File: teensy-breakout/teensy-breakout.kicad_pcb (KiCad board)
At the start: 2 copper layers, 1 part, among them U1 Teensy4.1

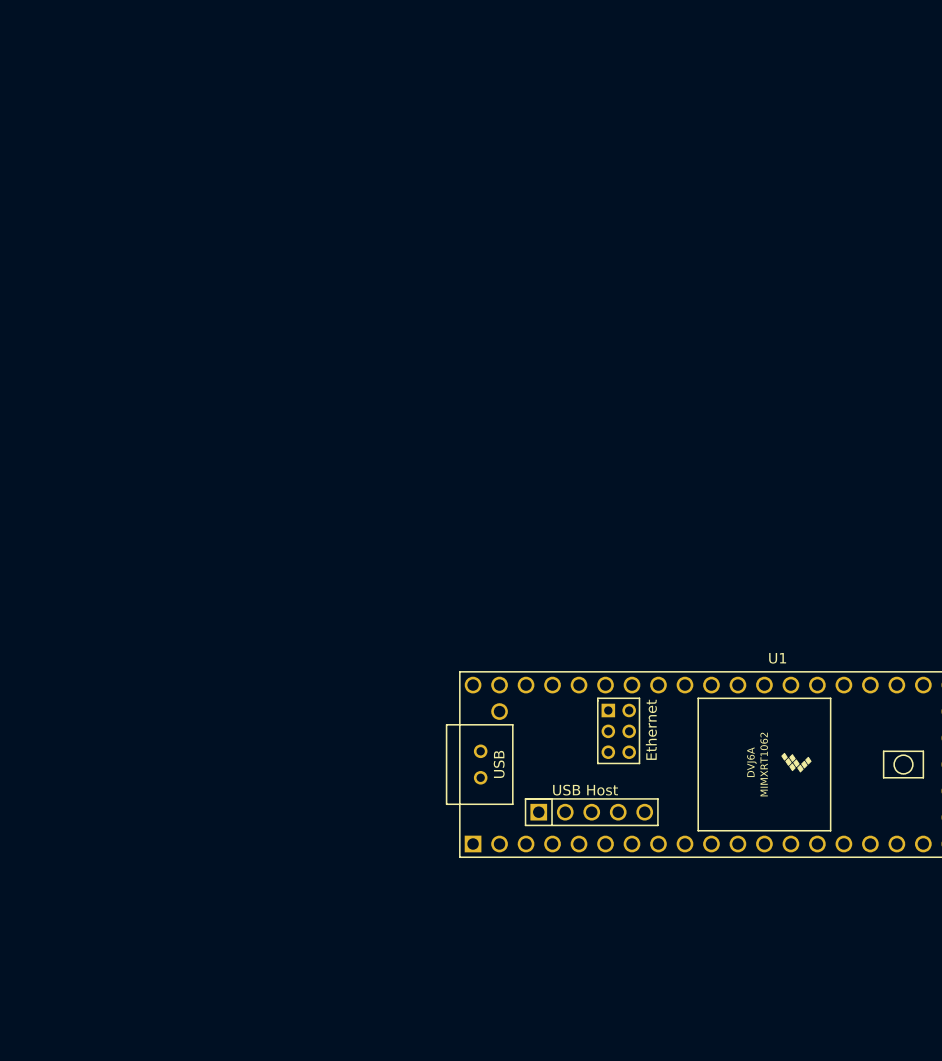
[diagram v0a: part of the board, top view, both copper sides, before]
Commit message: Initial work on teensy brakeout PCB
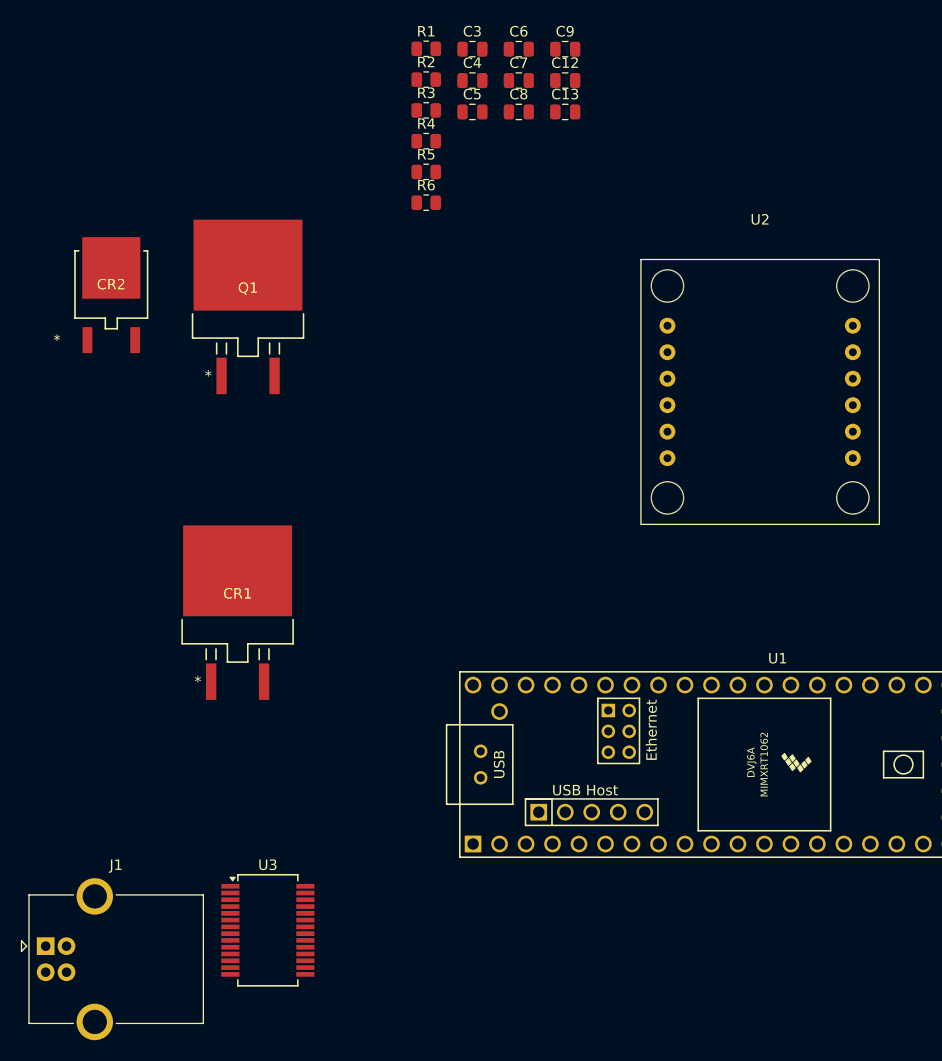
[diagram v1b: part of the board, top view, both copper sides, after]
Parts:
- added C12: 100n, Capacitor_SMD:C_0805_2012Metric, F.Cu at (85.9, 34.8)
- added C13: 10u, Capacitor_SMD:C_0805_2012Metric, F.Cu at (85.9, 37.8)
- added C3: 10u, Capacitor_SMD:C_0805_2012Metric, F.Cu at (77.0, 31.8)
- added C4: 1u, Capacitor_SMD:C_0805_2012Metric, F.Cu at (77.0, 34.8)
- added C5: 10u, Capacitor_SMD:C_0805_2012Metric, F.Cu at (77.0, 37.8)
- added C6: 1u, Capacitor_SMD:C_0805_2012Metric, F.Cu at (81.5, 31.8)
- added C7: 10u, Capacitor_SMD:C_0805_2012Metric, F.Cu at (81.5, 34.8)
- added C8: 10u, Capacitor_SMD:C_0805_2012Metric, F.Cu at (81.5, 37.8)
- added C9: 100n, Capacitor_SMD:C_0805_2012Metric, F.Cu at (85.9, 31.8)
- added CR1: L7805CD2T-TR, Custom:D2PAKSMD_2L_STD-ST_STM, F.Cu at (54.5, 84.0)
- added CR2: MBRD10100CT-13, Custom:TO252DPAK_DIO, F.Cu at (42.4, 54.3)
- added J1: USB_B, Connector_USB:USB_B_OST_USB-B1HSxx_Horizontal, F.Cu at (36.1, 117.8)
- added Q1: IRL530NSTRLPBF, Custom:D2PAKSMD_2L_STD-ST_STM, F.Cu at (55.5, 54.7)
- added R1: 1k, Resistor_SMD:R_0805_2012Metric, F.Cu at (72.6, 31.8)
- added R2: 10k, Resistor_SMD:R_0805_2012Metric, F.Cu at (72.6, 34.7)
- added R3: 270, Resistor_SMD:R_0805_2012Metric, F.Cu at (72.6, 37.6)
- added R4: 270, Resistor_SMD:R_0805_2012Metric, F.Cu at (72.6, 40.6)
- added R5: 2k, Resistor_SMD:R_0805_2012Metric, F.Cu at (72.6, 43.5)
- added R6: 2k, Resistor_SMD:R_0805_2012Metric, F.Cu at (72.6, 46.5)
- added U2: ~, Custom:BNO085, F.Cu at (104.6, 64.7)
- added U3: FT232RL, Package_SO:SSOP-28_5.3x10.2mm_P0.65mm, F.Cu at (57.4, 116.3)
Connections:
- U1 pad 1: unconnected-(U1-GND-Pad1) -> GND
- U1 pad 15: unconnected-(U1-3V3-Pad15) -> +3V3
- U1 pad 2: unconnected-(U1-0_RX1_CRX2_CS1-Pad2) -> /UART1 RX
- U1 pad 3: unconnected-(U1-1_TX1_CTX2_MISO1-Pad3) -> /UART1 TX
- U1 pad 34: unconnected-(U1-GND-Pad34) -> GND
- U1 pad 4: unconnected-(U1-2_OUT2-Pad4) -> /UART1 RTS
- U1 pad 40: unconnected-(U1-18_A4_SDA-Pad40) -> /I2C0_SDA
- U1 pad 41: unconnected-(U1-19_A5_SCL-Pad41) -> /I2C0_SCL
- U1 pad 46: unconnected-(U1-3V3-Pad46) -> +3V3
- U1 pad 47: unconnected-(U1-GND-Pad47) -> GND
- U1 pad 48: unconnected-(U1-VIN-Pad48) -> +5V
- U1 pad 5: unconnected-(U1-3_LRCLK2-Pad5) -> /UART1 CTS
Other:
- board outline added: 20.9 x 23.4 mm

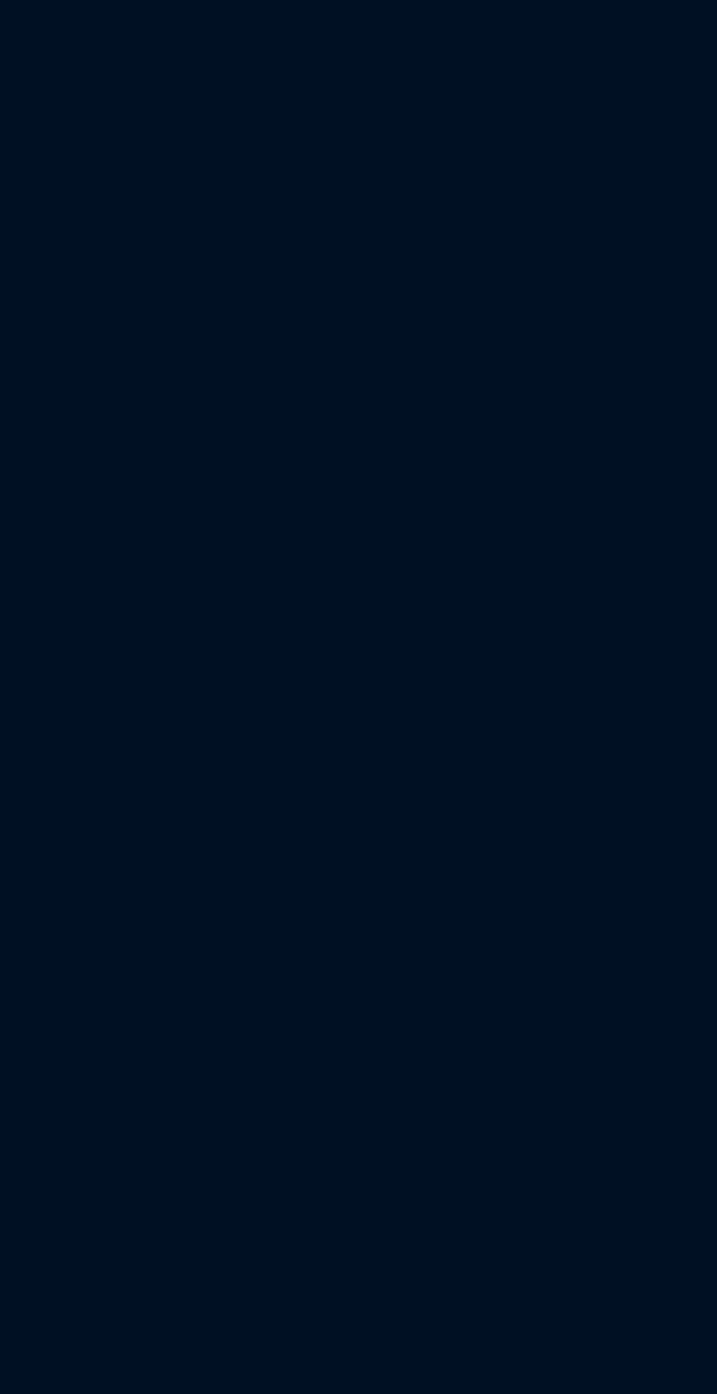
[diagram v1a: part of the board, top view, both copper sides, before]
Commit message: Started working to integrate ZED-F9P and feather. Still need to make Zed-F9P footprint.
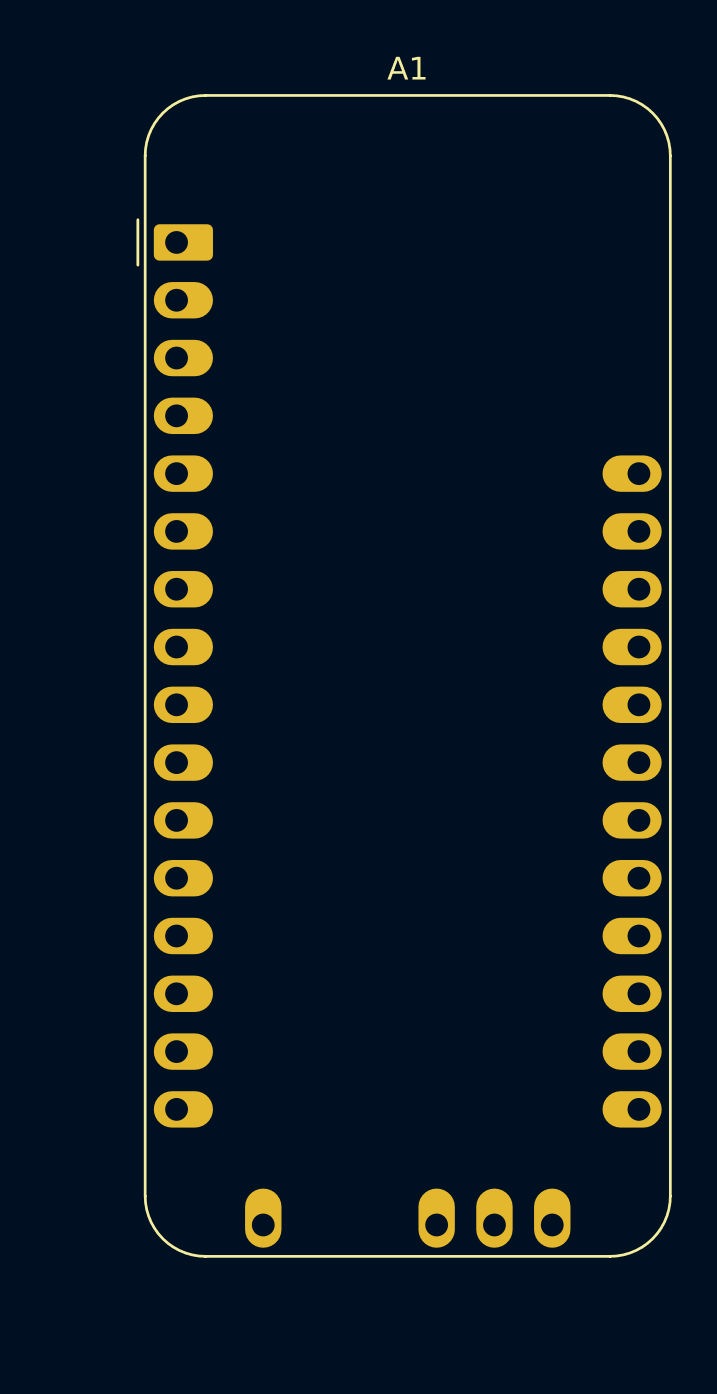
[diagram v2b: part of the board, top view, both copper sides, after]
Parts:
- added A1: Adafruit_Feather_M0_RFM9x_LoRa_Radio, Module:Adafruit_Feather_M0_RFM, F.Cu at (136.2, 30.4)

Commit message: More work done on schematic, seems good to me
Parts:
- added C14: 10u, Capacitor_SMD:C_0805_2012Metric_Pad1.18x1.45mm_HandSolder, F.Cu at (67.5, 31.4)
- added C15: 1u, Capacitor_SMD:C_0805_2012Metric_Pad1.18x1.45mm_HandSolder, F.Cu at (67.5, 34.4)
- added C16: 10u, Capacitor_SMD:C_0805_2012Metric_Pad1.18x1.45mm_HandSolder, F.Cu at (83.0, 44.0)
- added C17: 1u, Capacitor_SMD:C_0805_2012Metric_Pad1.18x1.45mm_HandSolder, F.Cu at (83.0, 47.0)
- added C18: 1u, Capacitor_SMD:C_0805_2012Metric_Pad1.18x1.45mm_HandSolder, F.Cu at (67.5, 37.5)
- added C19: 1u, Capacitor_SMD:C_0805_2012Metric_Pad1.18x1.45mm_HandSolder, F.Cu at (67.5, 40.5)
- added C20: 100u, Capacitor_SMD:C_0805_2012Metric_Pad1.18x1.45mm_HandSolder, F.Cu at (77.0, 40.5)
- added C21: 10u, Capacitor_SMD:C_0805_2012Metric_Pad1.18x1.45mm_HandSolder, F.Cu at (67.5, 43.5)
- added C22: 1u, Capacitor_SMD:C_0805_2012Metric_Pad1.18x1.45mm_HandSolder, F.Cu at (67.5, 46.5)
- added C23: 10u, Capacitor_SMD:C_0805_2012Metric_Pad1.18x1.45mm_HandSolder, F.Cu at (67.5, 49.5)
- added C24: 10u, Capacitor_SMD:C_0805_2012Metric_Pad1.18x1.45mm_HandSolder, F.Cu at (67.5, 52.5)
- added J10: 1988820, Custom:CONN_1988820, F.Cu at (53.7, 154.8)
- added J2: 1988820, Custom:CONN_1988820, F.Cu at (28.5, 82.2)
- added J3: 1988820, Custom:CONN_1988820, F.Cu at (28.5, 96.8)
- added J4: 1988820, Custom:CONN_1988820, F.Cu at (28.5, 111.4)
- added J5: 1988820, Custom:CONN_1988820, F.Cu at (28.5, 126.0)
- added J6: 1988820, Custom:CONN_1988820, F.Cu at (28.5, 140.6)
- added J7: 1988820, Custom:CONN_1988820, F.Cu at (28.5, 155.2)
- added J8: 1988833, Custom:CONN_1988833, F.Cu at (58.7, 140.2)
- added J9: 1988956, Custom:CONN_1988956, F.Cu at (64.3, 153.5)
- added R10: 10k, Resistor_SMD:R_0805_2012Metric_Pad1.20x1.40mm_HandSolder, F.Cu at (77.5, 51.0)
- added R8: 1k, Resistor_SMD:R_0805_2012Metric_Pad1.20x1.40mm_HandSolder, F.Cu at (77.5, 45.1)
- added R9: 10k, Resistor_SMD:R_0805_2012Metric_Pad1.20x1.40mm_HandSolder, F.Cu at (77.5, 48.0)
- added U5: ~, Custom:RFM69HCW Adafruit Breakout, F.Cu at (177.4, 115.4)
- added U6: ICL7667CBAZA-TDKR, Custom:SOIC8_4X5_INR, F.Cu at (61.3, 160.1)
- C12: value 100n -> 1u; footprint Capacitor_SMD:C_0805_2012Metric -> Capacitor_SMD:C_0805_2012Metric_Pad1.18x1.45mm_HandSolder
- C13, C3, C4, C5, C6, C7, C8, C9: footprint Capacitor_SMD:C_0805_2012Metric -> Capacitor_SMD:C_0805_2012Metric_Pad1.18x1.45mm_HandSolder
- R3, R4, R5, R6: footprint Resistor_SMD:R_0805_2012Metric -> Resistor_SMD:R_0805_2012Metric_Pad1.20x1.40mm_HandSolder
- moved U3 0.50 mm to (56.9, 116.3)
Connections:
- R1 pad 1: unconnected-(R1-Pad1) -> /BRAKE
- U1 pad 10: unconnected-(U1-8_TX2_IN1-Pad10) -> /UART2_TX
- U1 pad 12: unconnected-(U1-10_CS_MQSR-Pad12) -> /RF_CS
- U1 pad 13: unconnected-(U1-11_MOSI_CTX1-Pad13) -> /MOSI
- U1 pad 14: unconnected-(U1-12_MISO_MQSL-Pad14) -> /MISO
- U1 pad 18: unconnected-(U1-26_A12_MOSI1-Pad18) -> /BRAKE
- U1 pad 19: unconnected-(U1-27_A13_SCK1-Pad19) -> /PUL
- U1 pad 28: unconnected-(U1-36_CS-Pad28) -> /RF_G0
- U1 pad 29: unconnected-(U1-37_CS-Pad29) -> /RF_RST
- U1 pad 30: unconnected-(U1-38_CS1_IN1-Pad30) -> /DIR
- U1 pad 31: unconnected-(U1-39_MISO1_OUT1A-Pad31) -> /ALM
- U1 pad 35: unconnected-(U1-13_SCK_LED-Pad35) -> /SCK
- U1 pad 9: unconnected-(U1-7_RX2_OUT1A-Pad9) -> /UART2_RX
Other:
- board size 20.9 x 23.4 mm -> 25.4 x 29.2 mm

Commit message: Work on layout & wiring. Mostly done, need to look it over. It's very messy :(
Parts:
- added C1: 100u, Custom:CAP_A765EB_KEM, F.Cu at (188.2, 52.5)
- added C2: 100u, Custom:CAP_A765EB_KEM, F.Cu at (208.9, 66.5)
- added C25: 1u, Capacitor_SMD:C_0805_2012Metric_Pad1.18x1.45mm_HandSolder, F.Cu at (114.0, 35.5)
- added CR3: L7805CD2T-TR, Custom:D2PAKSMD_2L_STD-ST_STM, F.Cu at (213.5, 122.0)
- added CR4: L7805CD2T-TR, Custom:D2PAKSMD_2L_STD-ST_STM, F.Cu at (86.5, 80.5)
- added D1: BLUE, LED_SMD:LED_0805_2012Metric, F.Cu at (57.6, 72.1)
- added D2: BLUE, LED_SMD:LED_0805_2012Metric, F.Cu at (61.6, 72.0)
- added D3: LED, LED_SMD:LED_0805_2012Metric_Pad1.15x1.40mm_HandSolder, F.Cu at (227.4, 99.0)
- added D4: GREEN, LED_SMD:LED_0805_2012Metric, F.Cu at (107.4, 100.0)
- added J11: 1988817, Custom:CONN_1988817, F.Cu at (82.4, 30.2)
- added J12: 1988817, Custom:CONN_1988817, F.Cu at (16.5, 133.2)
- added J13: 1988817, Custom:CONN_1988817, F.Cu at (16.7, 178.6)
- added J14: 1988817, Custom:CONN_1988817, F.Cu at (72.6, 191.8)
- added J15: 1988820, Custom:CONN_1988820, F.Cu at (58.8, 30.0)
- added J17: 1988956, Custom:CONN_1988956, F.Cu at (251.3, 31.6)
- added J18: 1988817, Custom:CONN_1988817, F.Cu at (161.9, 30.2)
- added J19: 1989010, Custom:PHOENIX_1989010, F.Cu at (25.8, 194.4)
- added J20: 1989010, Custom:PHOENIX_1989010, F.Cu at (151.5, 27.6)
- added J21: 1988956, Custom:CONN_1988956, F.Cu at (186.4, 29.2)
- added J22: 1988817, Custom:CONN_1988817, F.Cu at (213.2, 191.5)
- added J9: 1988956, Custom:CONN_1988956, F.Cu at (251.3, 127.6)
- added R11: 2k, Resistor_SMD:R_0805_2012Metric_Pad1.20x1.40mm_HandSolder, F.Cu at (229.0, 36.5)
- added R12: 2k, Resistor_SMD:R_0805_2012Metric_Pad1.20x1.40mm_HandSolder, F.Cu at (229.0, 31.5)
- added R13: 120, Resistor_SMD:R_0805_2012Metric_Pad1.20x1.40mm_HandSolder, F.Cu at (113.5, 100.0)
- added R14: 200k, Resistor_SMD:R_0805_2012Metric_Pad1.20x1.40mm_HandSolder, F.Cu at (62.0, 65.0)
- added R15: 200k, Resistor_SMD:R_0805_2012Metric_Pad1.20x1.40mm_HandSolder, F.Cu at (76.9, 86.5)
- added R16: 200k, Resistor_SMD:R_0805_2012Metric_Pad1.20x1.40mm_HandSolder, F.Cu at (54.5, 173.0)
- added R7: 500, Resistor_SMD:R_0805_2012Metric_Pad1.20x1.40mm_HandSolder, F.Cu at (226.9, 162.5)
- added R8: 1k, Resistor_SMD:R_0805_2012Metric_Pad1.20x1.40mm_HandSolder, F.Cu at (233.5, 123.5)
- added SW1: 7101MD9AQE, Custom:SW3_7101MD9AQE_CNK, F.Cu at (210.4, 45.7)
- added U10: LSF0102DCUR, Custom:DCU0008A_M, F.Cu at (70.2, 79.3)
- added U4: ~, Custom:ZED F9P RTK SMA, F.Cu at (99.5, 173.8)
- added U7: LSF0102DCUR, Custom:DCU0008A_M, F.Cu at (51.0, 167.0)
- added U8: LSF0102DCUR, Custom:DCU0008A_M, F.Cu at (62.3, 58.8)
- C20: value 100u -> 1u
- moved J6 231.2 mm to (251.3, 78.9), turned to 90 degrees
- moved J2 224.3 mm to (251.2, 55.7), turned to 90 degrees
- moved J4 222.9 mm to (251.3, 103.7), turned to 90 degrees
- moved J9 216.6 mm to (251.3, 44.1), turned to 90 degrees
- moved J8 195.2 mm to (247.0, 191.5)
- moved CR2 185.3 mm to (224.7, 87.2)
- moved Q1 170.1 mm to (225.5, 61.1)
- moved C22 166.1 mm to (190.5, 158.0), turned to 180 degrees
- moved C21 163.7 mm to (190.5, 151.5), turned to 180 degrees
- moved R2 160.5 mm to (227.1, 78.0), turned to 180 degrees
- moved R1 156.0 mm to (221.6, 78.0)
- moved R8 154.1 mm to (221.9, 99.0), turned to -90 degrees
- moved U6 152.9 mm to (214.2, 160.4)
- moved C18 141.4 mm to (123.0, 167.5), turned to 90 degrees
- moved C14 139.1 mm to (128.5, 156.5), turned to -90 degrees
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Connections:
- net /MISO renamed /MISO0
- net /MOSI renamed /MOSI0
- net /SCK renamed /SCK0
- C16 pad 1: +5V -> +3V3
- CR1 pad 3: +5V -> Net-(CR1-OUTPUT)
- J6 pad 1: +5V -> Net-(CR3-OUTPUT)
- J6 pad 2: +5V -> Net-(CR3-OUTPUT)
- J6 pad 3: +5V -> Net-(CR3-OUTPUT)
- J6 pad 4: +5V -> Net-(CR3-OUTPUT)
- J7 pad 1: +5V -> Net-(CR3-OUTPUT)
- J7 pad 2: +5V -> Net-(CR3-OUTPUT)
- J7 pad 3: +5V -> Net-(CR3-OUTPUT)
- J7 pad 4: +5V -> Net-(CR3-OUTPUT)
- U1 pad 10: /UART2_TX -> /RC_TX
- U1 pad 11: unconnected-(U1-9_OUT1C-Pad11) -> /NP4
- U1 pad 16: unconnected-(U1-24_A10_TX6_SCL2-Pad16) -> /J0_1
- U1 pad 17: unconnected-(U1-25_A11_RX6_SDA2-Pad17) -> /J0_2
- U1 pad 18: /BRAKE -> /MOSI1
- U1 pad 19: /PUL -> /SCK1
- U1 pad 20: unconnected-(U1-28_RX7-Pad20) -> /J0_3
- U1 pad 21: unconnected-(U1-29_TX7-Pad21) -> /J0_4
- U1 pad 22: unconnected-(U1-30_CRX3-Pad22) -> /J0_5
- U1 pad 23: unconnected-(U1-31_CTX3-Pad23) -> /J0_6
- U1 pad 24: unconnected-(U1-32_OUT1B-Pad24) -> /J0_7
- U1 pad 25: unconnected-(U1-33_MCLK2-Pad25) -> /J0_8
- U1 pad 26: unconnected-(U1-34_RX8-Pad26) -> /J1_1
- U1 pad 27: unconnected-(U1-35_TX8-Pad27) -> /J1_2
- U1 pad 31: /ALM -> /MISO1
- U1 pad 32: unconnected-(U1-40_A16-Pad32) -> /J1_3
- U1 pad 33: unconnected-(U1-41_A17-Pad33) -> /J1_4
- U1 pad 36: unconnected-(U1-14_A0_TX3_SPDIF_OUT-Pad36) -> /J1_5
- U1 pad 37: unconnected-(U1-15_A1_RX3_SPDIF_IN-Pad37) -> /J1_6
- U1 pad 38: unconnected-(U1-16_A2_RX4_SCL1-Pad38) -> Net-(U1-16_A2_RX4_SCL1)
- U1 pad 39: unconnected-(U1-17_A3_TX4_SDA1-Pad39) -> Net-(U1-17_A3_TX4_SDA1)
- U1 pad 42: unconnected-(U1-20_A6_TX5_LRCLK1-Pad42) -> /J1_7
- U1 pad 43: unconnected-(U1-21_A7_RX5_BCLK1-Pad43) -> /ALM
- U1 pad 44: unconnected-(U1-22_A8_CTX1-Pad44) -> /BRAKE
- U1 pad 45: unconnected-(U1-23_A9_CRX1_MCLK1-Pad45) -> /PUL
- U1 pad 6: unconnected-(U1-4_BCLK2-Pad6) -> /NP1
- U1 pad 7: unconnected-(U1-5_IN2-Pad7) -> /NP2
- U1 pad 8: unconnected-(U1-6_OUT1D-Pad8) -> /NP3
- U1 pad 9: /UART2_RX -> /RC_RX
- U3 pad 15: unconnected-(U3-USBD+-Pad15) -> /USB_DP
- U3 pad 16: unconnected-(U3-USBD--Pad16) -> /USB_DM
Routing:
- net GND: track 0.00 -> 338.7 mm, vias 0 -> 18
- net Net-(CR4-OUTPUT): track 0.00 -> 314.9 mm, vias 0 -> 7
- net Net-(CR3-OUTPUT): track 0.00 -> 284.5 mm, vias 0 -> 4
- net /MOSI0: track 0.00 -> 239.5 mm, vias 0 -> 9
- net /MISO0: track 0.00 -> 233.1 mm, vias 0 -> 8
- net /ALM: track 0.00 -> 228.3 mm, vias 0 -> 7
- net /I2C0_SCL: track 0.00 -> 199.3 mm, vias 0 -> 10
- net /I2C0_SDA: track 0.00 -> 198.3 mm, vias 0 -> 12
- net /PUL: track 0.00 -> 190.0 mm, vias 0 -> 5
- net /SCK0: track 0.00 -> 189.5 mm, vias 0 -> 8
- net +12V: track 0.00 -> 180.5 mm, vias 0 -> 7
- net /SCK1: track 0.00 -> 179.3 mm, vias 0 -> 2
- net +5V: track 0.00 -> 178.8 mm, vias 0 -> 9
- net /MOSI1: track 0.00 -> 170.6 mm, vias 0 -> 3
- net /J0_2: track 0.00 -> 168.4 mm, vias 0 -> 2
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- added copper zone on In3.Cu, net +12V
- added copper zone on In2.Cu, net +3V3
- added copper zone on In4.Cu, net +5V
- added copper zone on In1.Cu, net GND
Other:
- board size 25.4 x 29.2 mm -> 240.5 x 168.5 mm
- copper layers 2 -> 6
- board text added: "+12V"
- board text added: "+3V3"
- board text added: "+3V3 GPIO"
- board text added: "+5V"
- board text added: "+5V GPIO"
- board text added: "ALM"
- board text added: "BRAKE SOLENOID"
- board text added: "Brake LED"
- board text added: "DIR_MIN"
- board text added: "DIR_PLUS"
- board text added: "GND"
- board text added: "I2C1"
- board text added: "L"
- board text added: "LIMIT SWITCHES"
- board text added: "MISO0"
- board text added: "MISO1"
- board text added: "MOSI0"
- board text added: "MOSI1"
- board text added: "OUT"
- board text added: "POWER INPUT"
- board text added: "POWER SWITCH"
- board text added: "PUL_MIN"
- board text added: "PUL_PLUS"
- board text added: "Power from CR3 linear regulator"
- board text added: "Power from CR4 linear regulator"
- board text added: "R"
- board text added: "RC STATION"
- board text added: "SCK0"
- board text added: "SCK1"
- board text added: "SCL1"
- board text added: "SDA1"
- board text added: "SPI0"
- board text added: "SPI1"
- board text added: "STEPPER CONTROL"
- board text added: "TEENSY_RX"
- board text added: "TEENSY_TX"
